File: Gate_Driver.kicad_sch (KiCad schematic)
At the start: 22 parts, among them J1 171857-0002, J2 171857-0002

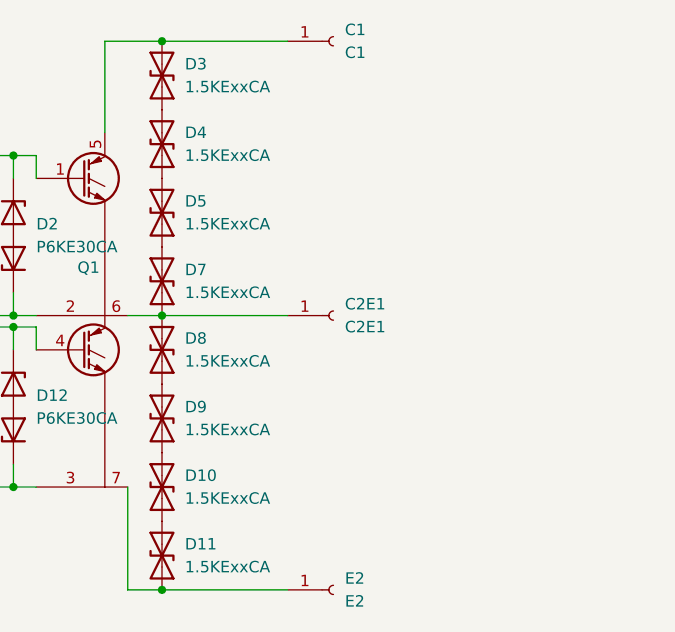
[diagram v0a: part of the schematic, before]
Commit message: Design done with smaller cap
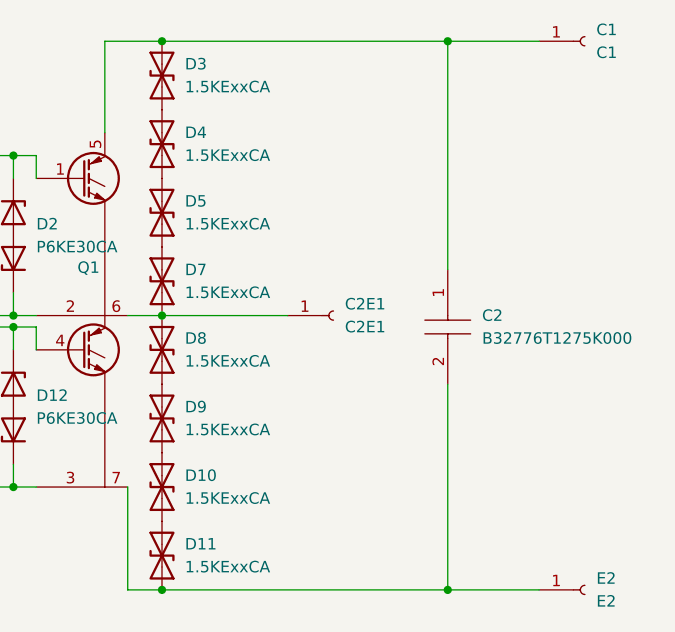
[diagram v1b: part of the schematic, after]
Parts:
- added C2: B32776T1275K000, B32776T1275K000, symbol SamacSys_Parts:B32776T1275K000
- C1, C2E1, E2: footprint Connector_Wire:SolderWirePad_1x01_SMD_5x10mm -> Library:Custom CM300DU Terminal Connector
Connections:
- net at D11.1 (A1), E2.1 (Pin_1), Q1.7 (E2): now also C2.2
- net at C1.1 (Pin_1), D3.2 (A2), Q1.5 (C1): now also C2.1
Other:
- moved on the sheet: C1, E2
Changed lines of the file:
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@@
+	)
+	(junction
+		(at 144.78 17.78)
+		(diameter 0)
+		(color 0 0 0 0)
 	)
 	(junction
@@
 	)
 	(junction
+		(at 144.78 78.74)
+		(diameter 0)
+		(color 0 0 0 0)
+	)
+	(junction
 		(at 77.47 49.53)
 		(diameter 0)
@@
 	(wire
 		(pts
+			(xy 144.78 17.78) (xy 144.78 43.18)
+		)
+		(stroke
+			(width 0)
+			(type default)
+		)
+	)
+	(wire
+		(pts
+			(xy 144.78 55.88) (xy 144.78 78.74)
+		)
+		(stroke
+			(width 0)
+			(type default)
+		)
+	)
+	(wire
+		(pts
 			(xy 109.22 78.74) (xy 109.22 67.31)
 		)
@@
 	(wire
 		(pts
+			(xy 144.78 78.74) (xy 154.94 78.74)
+		)
+		(stroke
+			(width 0)
+			(type default)
+		)
+	)
+	(wire
+		(pts
 			(xy 106.68 17.78) (xy 113.03 17.78)
 		)
@@
 	(wire
 		(pts
-			(xy 113.03 17.78) (xy 127 17.78)
+			(xy 113.03 17.78) (xy 144.78 17.78)
 		)
 		(stroke
@@
 	(wire
 		(pts
-			(xy 113.03 78.74) (xy 127 78.74)
+			(xy 113.03 78.74) (xy 144.78 78.74)
 		)
 		(stroke
@@
 		(pts
 			(xy 74.93 57.15) (xy 72.39 57.15)
+		)
+		(stroke
+			(width 0)
+			(type default)
+		)
+	)
+	(wire
+		(pts
+			(xy 144.78 17.78) (xy 154.94 17.78)
 		)
 		(stroke
@@
 			)
 		)
-		(property "Footprint" "Connector_Wire:SolderWirePad_1x01_SMD_5x10mm"
+		(property "Footprint" "Library:Custom CM300DU Terminal Connector"
 			(at 132.08 48.26 0)
 			(effects
@@
 	(symbol
 		(lib_id "Connector:Conn_01x01_Socket")
-		(at 132.08 17.78 0)
+		(at 160.02 17.78 0)
 		(unit 1)
 		(exclude_from_sim no)
@@
 		(fields_autoplaced yes)
 		(property "Reference" "C1"
-			(at 133.35 16.5099 0)
+			(at 161.29 16.5099 0)
 			(effects
 				(font
@@
 		)
 		(property "Value" "C1"
-			(at 133.35 19.0499 0)
-			(effects
-				(font
-					(size 1.27 1.27)
-				)
-				(justify left)
-			)
-		)
-		(property "Footprint" "Connector_Wire:SolderWirePad_1x01_SMD_5x10mm"
-			(at 132.08 17.78 0)
+			(at 161.29 19.0499 0)
+			(effects
+				(font
+					(size 1.27 1.27)
+				)
+				(justify left)
+			)
+		)
+		(property "Footprint" "Library:Custom CM300DU Terminal Connector"
+			(at 160.02 17.78 0)
 			(effects
 				(font
@@
 		)
 		(property "Datasheet" "~"
-			(at 132.08 17.78 0)
+			(at 160.02 17.78 0)
 			(effects
 				(font
@@
 		)
 		(property "Description" "Generic connector, single row, 01x01, script generated"
-			(at 132.08 17.78 0)
+			(at 160.02 17.78 0)
 			(effects
 				(font
@@
 	)
 	(symbol
+		(lib_id "SamacSys_Parts:B32776T1275K000")
+		(at 144.78 43.18 270)
+		(unit 1)
+		(exclude_from_sim no)
+		(in_bom yes)
+		(on_board yes)
+		(dnp no)
+		(fields_autoplaced yes)
+		(property "Reference" "C2"
+			(at 148.59 48.2599 90)
+			(effects
+				(font
+					(size 1.27 1.27)
+				)
+				(justify left)
+			)
+		)
+		(property "Value" "B32776T1275K000"
+			(at 148.59 50.7999 90)
+			(effects
+				(font
+					(size 1.27 1.27)
+				)
+				(justify left)
+			)
+		)
+		(property "Footprint" "B32776T1275K000"
+			(at 146.05 52.07 0)
+			(effects
+				(font
+					(size 1.27 1.27)
+				)
+				(justify left)
+				(hide yes)
+			)
+		)
+		(property "Datasheet" "https://product.tdk.com/system/files/dam/doc/product/capacitor/film/mkp_mfp/data_sheet/20/20/db/fc_2009/mkp_b32774_778.pdf"
+			(at 143.51 52.07 0)
+			(effects
+				(font
+					(size 1.27 1.27)
+				)
+				(justify left)
+				(hide yes)
+			)
+		)
+		(property "Description" "Metallized Polypropylene Capacitors (MKP/MFP), 2.7uF, 1300V DC, 24mm(W) x 15mm(H) x 41.5mm(L)"
+			(at 144.78 43.18 0)
+			(effects
+				(font
+					(size 1.27 1.27)
+				)
+				(hide yes)
+			)
+		)
+		(property "Description_1" "Metallized Polypropylene Capacitors (MKP/MFP), 2.7uF, 1300V DC, 24mm(W) x 15mm(H) x 41.5mm(L)"
+			(at 140.97 52.07 0)
+			(effects
+				(font
+					(size 1.27 1.27)
+				)
+				(justify left)
+				(hide yes)
+			)
+		)
+		(property "Height" "15"
+			(at 138.43 52.07 0)
+			(effects
+				(font
+					(size 1.27 1.27)
+				)
+				(justify left)
+				(hide yes)
+			)
+		)
+		(property "Mouser Part Number" "871-B32776T1275K000"
+			(at 135.89 52.07 0)
+			(effects
+				(font
+					(size 1.27 1.27)
+				)
+				(justify left)
+				(hide yes)
+			)
+		)
+		(property "Mouser Price/Stock" "https://www.mouser.co.uk/ProductDetail/EPCOS-TDK/B32776T1275K000?qs=BZBei1rCqCAArBWXPfIatA%3D%3D"
+			(at 133.35 52.07 0)
+			(effects
+				(font
+					(size 1.27 1.27)
+				)
+				(justify left)
+				(hide yes)
+			)
+		)
+		(property "Manufacturer_Name" "TDK"
+			(at 130.81 52.07 0)
+			(effects
+				(font
+					(size 1.27 1.27)
+				)
+				(justify left)
+				(hide yes)
+			)
+		)
+		(property "Manufacturer_Part_Number" "B32776T1275K000"
+			(at 128.27 52.07 0)
+			(effects
+				(font
+					(size 1.27 1.27)
+				)
+				(justify left)
+				(hide yes)
+			)
+		)
+		(pin "2"
+		)
+		(pin "1"
+		)
+		(instances
+			(project ""
+				(path "/dbc28b68-3a1b-436d-82f3-9b167f62e8e3"
+					(reference "C2")
+					(unit 1)
+				)
+			)
+		)
+	)
+	(symbol
 		(lib_id "Diode:1N5819")
 		(at 81.28 33.02 0)
@@
 	(symbol
 		(lib_id "Connector:Conn_01x01_Socket")
-		(at 132.08 78.74 0)
+		(at 160.02 78.74 0)
 		(unit 1)
 		(exclude_from_sim no)
@@
 		(fields_autoplaced yes)
 		(property "Reference" "E2"
-			(at 133.35 77.4699 0)
+			(at 161.29 77.4699 0)
 			(effects
 				(font
@@
 		)
 		(property "Value" "E2"
-			(at 133.35 80.0099 0)
-			(effects
-				(font
-					(size 1.27 1.27)
-				)
-				(justify left)
-			)
-		)
-		(property "Footprint" "Connector_Wire:SolderWirePad_1x01_SMD_5x10mm"
-			(at 132.08 78.74 0)
+			(at 161.29 80.0099 0)
+			(effects
+				(font
+					(size 1.27 1.27)
+				)
+				(justify left)
+			)
+		)
+		(property "Footprint" "Library:Custom CM300DU Terminal Connector"
+			(at 160.02 78.74 0)
 			(effects
 				(font
@@
 		)
 		(property "Datasheet" "~"
-			(at 132.08 78.74 0)
+			(at 160.02 78.74 0)
 			(effects
 				(font
@@
 		)
 		(property "Description" "Generic connector, single row, 01x01, script generated"
-			(at 132.08 78.74 0)
-			(effects
-				(font
+			(at 160.02 78.74 0)
+			(effects
+				(font

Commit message: minor tweaks
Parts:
- removed C2: B32776T1275K000, B32776T1275K000, symbol SamacSys_Parts:B32776T1275K000
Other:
- moved on the sheet: C1, E2
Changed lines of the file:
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@@
-	)
-	(junction
-		(at 144.78 17.78)
-		(diameter 0)
-		(color 0 0 0 0)
 	)
 	(junction
@@
 	)
 	(junction
-		(at 113.03 17.78)
-		(diameter 0)
-		(color 0 0 0 0)
-	)
-	(junction
 		(at 85.09 49.53)
 		(diameter 0)
@@
 	)
 	(junction
-		(at 96.52 49.53)
+		(at 113.03 17.78)
 		(diameter 0)
 		(color 0 0 0 0)
 	)
 	(junction
-		(at 144.78 78.74)
+		(at 113.03 78.74)
+		(diameter 0)
+		(color 0 0 0 0)
+	)
+	(junction
+		(at 96.52 49.53)
 		(diameter 0)
 		(color 0 0 0 0)
@@
 		(color 0 0 0 0)
 	)
-	(junction
-		(at 113.03 78.74)
-		(diameter 0)
-		(color 0 0 0 0)
-	)
 	(wire
 		(pts
@@
 	(wire
 		(pts
-			(xy 144.78 17.78) (xy 144.78 43.18)
-		)
-		(stroke
-			(width 0)
-			(type default)
-		)
-	)
-	(wire
-		(pts
-			(xy 144.78 55.88) (xy 144.78 78.74)
-		)
-		(stroke
-			(width 0)
-			(type default)
-		)
-	)
-	(wire
-		(pts
 			(xy 109.22 78.74) (xy 109.22 67.31)
 		)
@@
 	(wire
 		(pts
+			(xy 113.03 78.74) (xy 128.27 78.74)
+		)
+		(stroke
+			(width 0)
+			(type default)
+		)
+	)
+	(wire
+		(pts
 			(xy 69.85 58.42) (xy 74.93 58.42)
 		)
@@
 	(wire
 		(pts
-			(xy 144.78 78.74) (xy 154.94 78.74)
+			(xy 113.03 17.78) (xy 128.27 17.78)
 		)
 		(stroke
@@
 	(wire
 		(pts
-			(xy 113.03 17.78) (xy 144.78 17.78)
-		)
-		(stroke
-			(width 0)
-			(type default)
-		)
-	)
-	(wire
-		(pts
 			(xy 85.09 49.53) (xy 85.09 52.07)
 		)
@@
 	(wire
 		(pts
-			(xy 113.03 78.74) (xy 144.78 78.74)
-		)
-		(stroke
-			(width 0)
-			(type default)
-		)
-	)
-	(wire
-		(pts
 			(xy 85.09 30.48) (xy 85.09 33.02)
 		)
@@
 		(pts
 			(xy 74.93 57.15) (xy 72.39 57.15)
-		)
-		(stroke
-			(width 0)
-			(type default)
-		)
-	)
-	(wire
-		(pts
-			(xy 144.78 17.78) (xy 154.94 17.78)
 		)
 		(stroke
@@
 	(symbol
 		(lib_id "Connector:Conn_01x01_Socket")
-		(at 160.02 17.78 0)
+		(at 133.35 17.78 0)
 		(unit 1)
 		(exclude_from_sim no)
@@
 		(fields_autoplaced yes)
 		(property "Reference" "C1"
-			(at 161.29 16.5099 0)
+			(at 134.62 16.5099 0)
 			(effects
 				(font
@@
 		)
 		(property "Value" "C1"
-			(at 161.29 19.0499 0)
+			(at 134.62 19.0499 0)
 			(effects
 				(font
@@
 		)
 		(property "Footprint" "Library:Custom CM300DU Terminal Connector"
-			(at 160.02 17.78 0)
+			(at 133.35 17.78 0)
 			(effects
 				(font
@@
 		)
 		(property "Datasheet" "~"
-			(at 160.02 17.78 0)
+			(at 133.35 17.78 0)
 			(effects
 				(font
@@
 		)
 		(property "Description" "Generic connector, single row, 01x01, script generated"
-			(at 160.02 17.78 0)
+			(at 133.35 17.78 0)
 			(effects
 				(font
@@
 	)
 	(symbol
-		(lib_id "SamacSys_Parts:B32776T1275K000")
-		(at 144.78 43.18 270)
-		(unit 1)
-		(exclude_from_sim no)
-		(in_bom yes)
-		(on_board yes)
-		(dnp no)
-		(fields_autoplaced yes)
-		(property "Reference" "C2"
-			(at 148.59 48.2599 90)
-			(effects
-				(font
-					(size 1.27 1.27)
-				)
-				(justify left)
-			)
-		)
-		(property "Value" "B32776T1275K000"
-			(at 148.59 50.7999 90)
-			(effects
-				(font
-					(size 1.27 1.27)
-				)
-				(justify left)
-			)
-		)
-		(property "Footprint" "B32776T1275K000"
-			(at 146.05 52.07 0)
-			(effects
-				(font
-					(size 1.27 1.27)
-				)
-				(justify left)
-				(hide yes)
-			)
-		)
-		(property "Datasheet" "https://product.tdk.com/system/files/dam/doc/product/capacitor/film/mkp_mfp/data_sheet/20/20/db/fc_2009/mkp_b32774_778.pdf"
-			(at 143.51 52.07 0)
-			(effects
-				(font
-					(size 1.27 1.27)
-				)
-				(justify left)
-				(hide yes)
-			)
-		)
-		(property "Description" "Metallized Polypropylene Capacitors (MKP/MFP), 2.7uF, 1300V DC, 24mm(W) x 15mm(H) x 41.5mm(L)"
-			(at 144.78 43.18 0)
-			(effects
-				(font
-					(size 1.27 1.27)
-				)
-				(hide yes)
-			)
-		)
-		(property "Description_1" "Metallized Polypropylene Capacitors (MKP/MFP), 2.7uF, 1300V DC, 24mm(W) x 15mm(H) x 41.5mm(L)"
-			(at 140.97 52.07 0)
-			(effects
-				(font
-					(size 1.27 1.27)
-				)
-				(justify left)
-				(hide yes)
-			)
-		)
-		(property "Height" "15"
-			(at 138.43 52.07 0)
-			(effects
-				(font
-					(size 1.27 1.27)
-				)
-				(justify left)
-				(hide yes)
-			)
-		)
-		(property "Mouser Part Number" "871-B32776T1275K000"
-			(at 135.89 52.07 0)
-			(effects
-				(font
-					(size 1.27 1.27)
-				)
-				(justify left)
-				(hide yes)
-			)
-		)
-		(property "Mouser Price/Stock" "https://www.mouser.co.uk/ProductDetail/EPCOS-TDK/B32776T1275K000?qs=BZBei1rCqCAArBWXPfIatA%3D%3D"
-			(at 133.35 52.07 0)
-			(effects
-				(font
-					(size 1.27 1.27)
-				)
-				(justify left)
-				(hide yes)
-			)
-		)
-		(property "Manufacturer_Name" "TDK"
-			(at 130.81 52.07 0)
-			(effects
-				(font
-					(size 1.27 1.27)
-				)
-				(justify left)
-				(hide yes)
-			)
-		)
-		(property "Manufacturer_Part_Number" "B32776T1275K000"
-			(at 128.27 52.07 0)
-			(effects
-				(font
-					(size 1.27 1.27)
-				)
-				(justify left)
-				(hide yes)
-			)
-		)
-		(pin "2"
-		)
-		(pin "1"
-		)
-		(instances
-			(project ""
-				(path "/dbc28b68-3a1b-436d-82f3-9b167f62e8e3"
-					(reference "C2")
-					(unit 1)
-				)
-			)
-		)
-	)
-	(symbol
 		(lib_id "Diode:1N5819")
 		(at 81.28 33.02 0)
@@
 	(symbol
 		(lib_id "Connector:Conn_01x01_Socket")
-		(at 160.02 78.74 0)
+		(at 133.35 78.74 0)
 		(unit 1)
 		(exclude_from_sim no)
@@
 		(fields_autoplaced yes)
 		(property "Reference" "E2"
-			(at 161.29 77.4699 0)
+			(at 134.62 77.4699 0)
 			(effects
 				(font
@@
 		)
 		(property "Value" "E2"
-			(at 161.29 80.0099 0)
+			(at 134.62 80.0099 0)
 			(effects
 				(font
@@
 		)
 		(property "Footprint" "Library:Custom CM300DU Terminal Connector"
-			(at 160.02 78.74 0)
+			(at 133.35 78.74 0)
 			(effects
 				(font
@@
 		)
 		(property "Datasheet" "~"
-			(at 160.02 78.74 0)
+			(at 133.35 78.74 0)
 			(effects
 				(font
@@
 		)
 		(property "Description" "Generic connector, single row, 01x01, script generated"
-			(at 160.02 78.74 0)
-			(effects
-				(font
+			(at 133.35 78.74 0)
+			(effects
+				(font

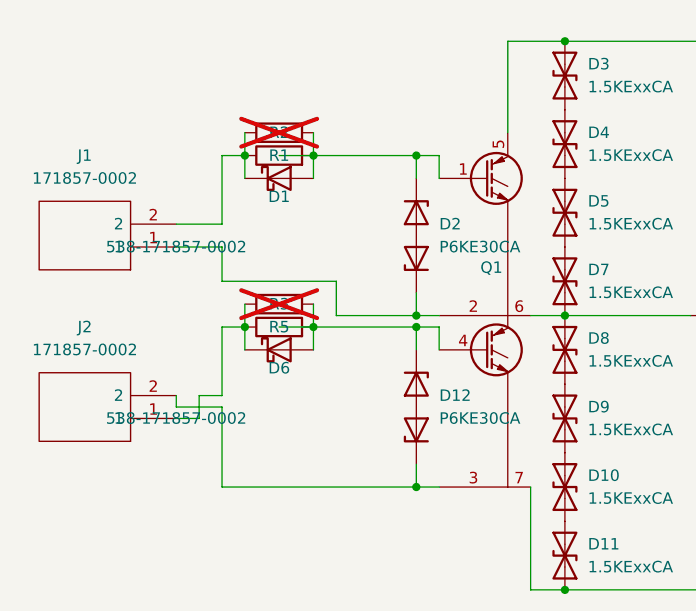
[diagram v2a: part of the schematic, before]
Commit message: Added pots and re-routed
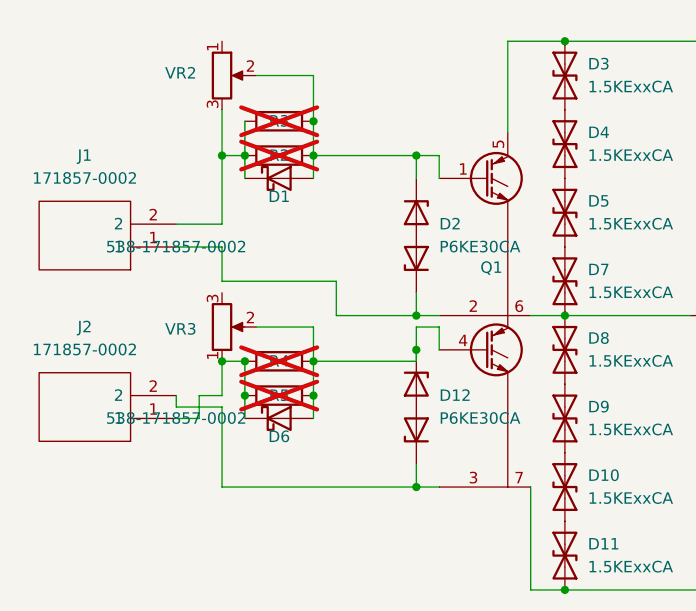
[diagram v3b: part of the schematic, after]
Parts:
- removed R1: 5.1, Resistor_THT:R_Axial_DIN0207_L6.3mm_D2.5mm_P10.16mm_Horizontal, symbol Device:R
- added R3: R, Resistor_SMD:R_0805_2012Metric_Pad1.20x1.40mm_HandSolder, symbol Device:R
- added VR2, VR3: 3362X-1-100LF, 3362X1100LF, symbol SamacSys_Parts:3362X-1-100LF
- R2: footprint Resistor_THT:R_Axial_DIN0207_L6.3mm_D2.5mm_P10.16mm_Horizontal -> Resistor_SMD:R_0805_2012Metric_Pad1.20x1.40mm_HandSolder
- R4: renamed from R3; footprint Resistor_THT:R_Axial_DIN0207_L6.3mm_D2.5mm_P10.16mm_Horizontal -> Resistor_SMD:R_0805_2012Metric_Pad1.20x1.40mm_HandSolder
- R5: value 5.1 -> R; footprint Resistor_THT:R_Axial_DIN0207_L6.3mm_D2.5mm_P10.16mm_Horizontal -> Resistor_SMD:R_0805_2012Metric_Pad1.20x1.40mm_HandSolder; now not fitted
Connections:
- net at D6.1 (K), J2.1, R4.1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: now also VR3.1
- net at D12.1 (K), D6.2 (A), Q1.4 (G2)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: now also VR3.2
- net at D1.2 (A), D2.1 (K), Q1.1 (G1)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: now also R3.2, VR2.2
- net at D1.1 (K), J1.2, R2.1: now also R3.1, VR2.3
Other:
- moved on the sheet: D6, R2, R4

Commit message: Clean up bom and minor PCB changes
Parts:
- C1, C2E1, E2, R2, R3, R4, R5: now left out of the parts list
- D1, D6: Mouser Part Number (none) -> 511-1N5819
- D10, D11, D3, D4, D5, D7, D8, D9: value 1.5KExxCA -> 1.5KE220CA; Mouser Part Number (none) -> 833-1.5KE220CA-TP
- D12, D2: Mouser Number 821-P6KE30CA -> (none); Mouser Part Number (none) -> 821-P6KE30CA
- J1, J2: Mouser Number 538-171857-0002 -> (none); Mouser Part Number (none) -> 538-171857-0002
- Q1: Mouser Part Number (none) -> 917-CM300DU-24NFH
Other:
- moved on the sheet: C1, C2E1, D1, D10, D11, D12, D2, D3, D4, D5, D6, D7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

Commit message: Route longer C1-E1 trace as a filled zone
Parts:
- added J3, J4: 22-01-2021, symbol Connector:Conn_01x02_Socket
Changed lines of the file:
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@@
+	)
+	(symbol
+		(lib_id "Connector:Conn_01x02_Socket")
+		(at 99.06 88.9 0)
+		(unit 1)
+		(exclude_from_sim no)
+		(in_bom yes)
+		(on_board no)
+		(dnp no)
+		(property "Reference" "J3"
+			(at 94.996 85.852 0)
+			(effects
+				(font
+					(size 1.27 1.27)
+				)
+				(justify left)
+			)
+		)
+		(property "Value" "22-01-2021"
+			(at 87.376 93.472 0)
+			(effects
+				(font
+					(size 1.27 1.27)
+				)
+				(justify left)
+				(hide yes)
+			)
+		)
+		(property "Footprint" ""
+			(at 99.06 88.9 0)
+			(effects
+				(font
+					(size 1.27 1.27)
+				)
+				(hide yes)
+			)
+		)
+		(property "Datasheet" "https://www.molex.com/en-us/products/part-detail-pdf/22012021?display=pdf"
+			(at 99.06 88.9 0)
+			(effects
+				(font
+					(size 1.27 1.27)
+				)
+				(hide yes)
+			)
+		)
+		(property "Description" "KK 254 Crimp Housing, 2 Circuits, Natural"
+			(at 99.06 88.9 0)
+			(effects
+				(font
+					(size 1.27 1.27)
+				)
+				(hide yes)
+			)
+		)
+		(property "Mouser Part Number" "538-22-01-2021 "
+			(at 99.06 88.9 0)
+			(effects
+				(font
+					(size 1.27 1.27)
+				)
+				(hide yes)
+			)
+		)
+		(pin "1"
+		)
+		(pin "2"
+		)
+		(instances
+			(project ""
+				(path "/dbc28b68-3a1b-436d-82f3-9b167f62e8e3"
+					(reference "J3")
+					(unit 1)
+				)
+			)
+		)
 	)
 	(symbol
@@
 					(unit 1)
 				)
+			)
+		)
+	)
+	(symbol
+		(lib_id "Connector:Conn_01x02_Socket")
+		(at 99.06 107.95 0)
+		(unit 1)
+		(exclude_from_sim no)
+		(in_bom yes)
+		(on_board no)
+		(dnp no)
+		(property "Reference" "J4"
+			(at 94.996 104.902 0)
+			(effects
+				(font
+					(size 1.27 1.27)
+				)
+				(justify left)
+			)
+		)
+		(property "Value" "22-01-2021"
+			(at 87.376 112.522 0)
+			(effects
+				(font
+					(size 1.27 1.27)
+				)
+				(justify left)
+				(hide yes)
+			)
+		)
+		(property "Footprint" ""
+			(at 99.06 107.95 0)
+			(effects
+				(font
+					(size 1.27 1.27)
+				)
+				(hide yes)
+			)
+		)
+		(property "Datasheet" "https://www.molex.com/en-us/products/part-detail-pdf/22012021?display=pdf"
+			(at 99.06 107.95 0)
+			(effects
+				(font
+					(size 1.27 1.27)
+				)
+				(hide yes)
+			)
+		)
+		(property "Description" "KK 254 Crimp Housing, 2 Circuits, Natural"
+			(at 99.06 107.95 0)
+			(effects
+				(font
+					(size 1.27 1.27)
+				)
+				(hide yes)
+			)
+		)
+		(property "Mouser Part Number" "538-22-01-2021 "
+			(at 99.06 107.95 0)
+			(effects
+				(font
+					(size 1.27 1.27)
+				)
+				(hide yes)
+			)
+		)
+		(pin "1"
+		)
+		(pin "2"
+		)
+		(instances
+			(project "Gate_Driver"
+				(path "/dbc28b68-3a1b-436d-82f3-9b167f62e8e3"
+					(reference "J4")
+					(unit 1)
+				)
